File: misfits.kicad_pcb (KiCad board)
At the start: 4 copper layers, 40 x 30 mm, 43 parts, among them J1 GT-USB-7010B, J2 S2B-PH-K-S_LF__SN_, J3 FH34SRJ-24S-0.5SH_50_, Q1 2N7002K-7, U1 ESP32-S3-MINI-1-N8, U2 BQ24040DSQR, U3 TLV75801PDRVR, U4 ESD7104MUTAG

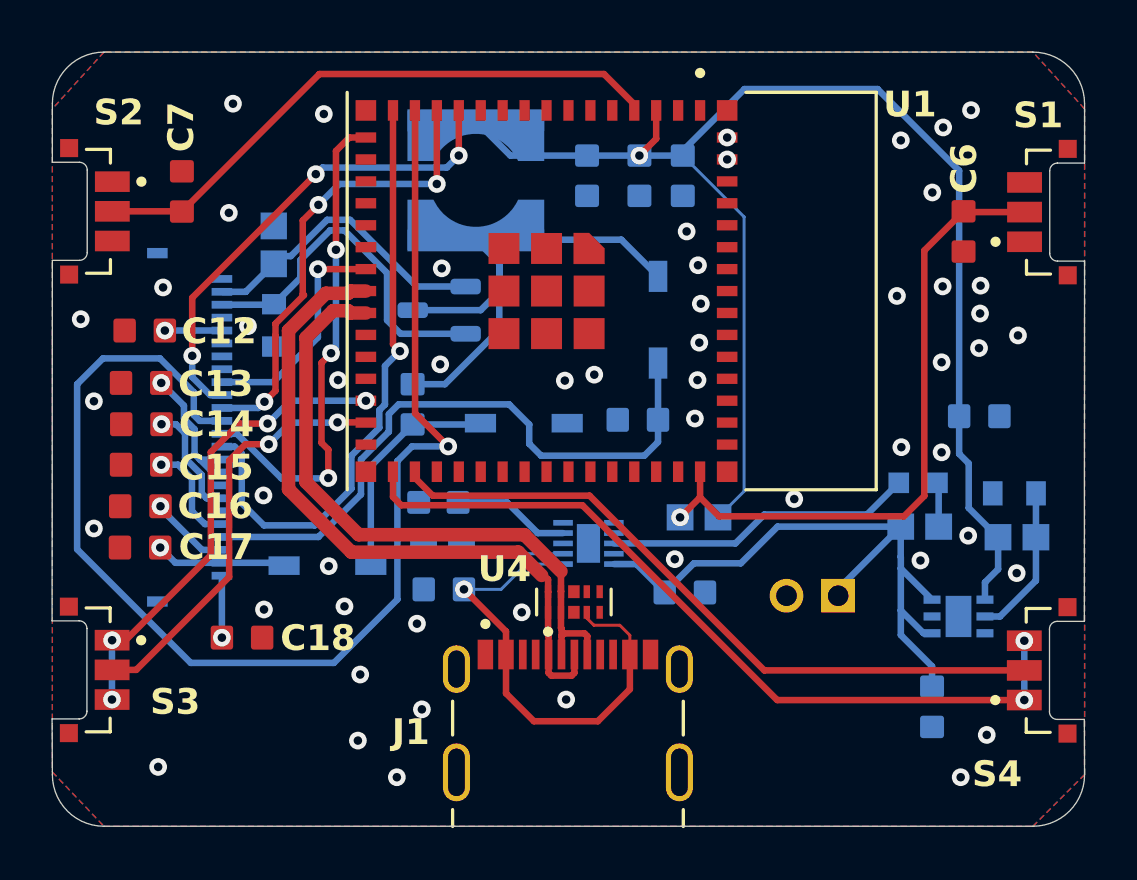
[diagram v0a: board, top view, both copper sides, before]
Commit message: Fix wrong resistor value, change font and orient text correctly
Signed-off-by: Lucy Mielke <user@domain.tld>
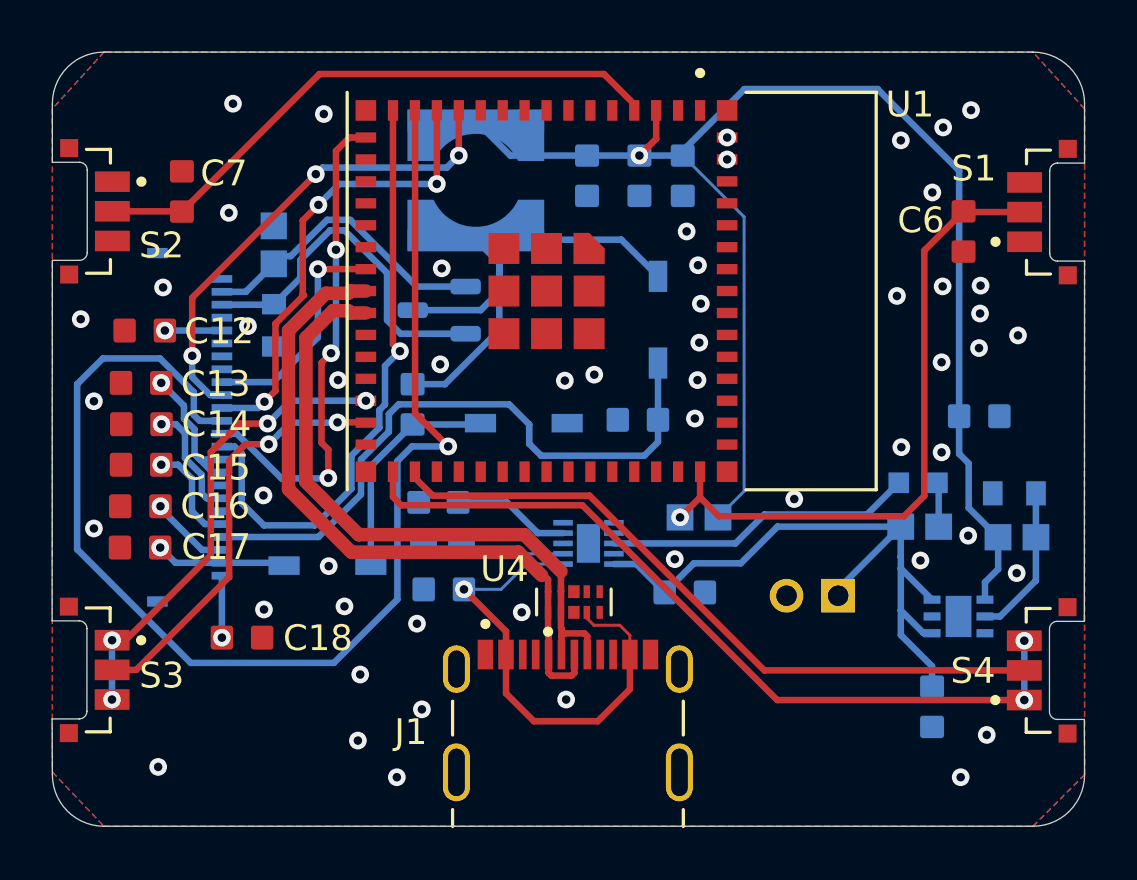
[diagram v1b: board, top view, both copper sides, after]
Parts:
- C11, C9: value 0.47uF -> 4.7uF
- R2: value 2k -> 2K
- R6: value 200k -> 200K Ohms
- R8: value 2.2k -> 2.2R
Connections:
- U3 pad 7: GND -> (no net)
- U4 pad 10: /USB_D_N -> (no net)
- U4 pad 9: /USB_D_P -> (no net)

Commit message: Parameterize schematic/PCB layout metadata
Signed-off-by: Lucy Mielke <user@domain.tld>
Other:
- board text added: "${TITLE} rev ${REVISION} ${CURRENT_DATE} ${COMMENT1}"
- board text removed: "{dblquote}Misfits{dblquote} Rev 2 14.03.2026"
